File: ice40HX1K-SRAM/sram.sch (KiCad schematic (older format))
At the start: 1 part

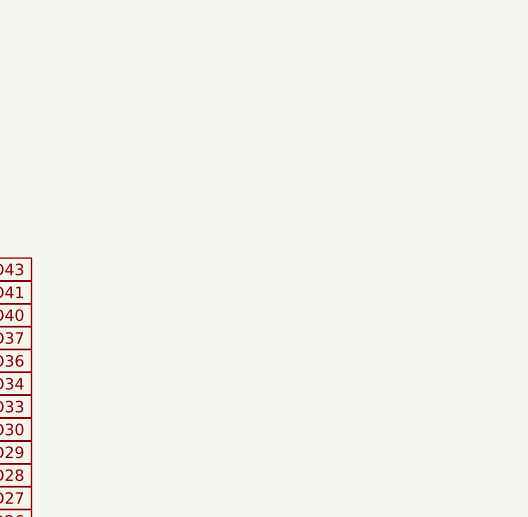
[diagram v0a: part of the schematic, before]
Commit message: Started USB => ice40 HX1K Bridge with ATSAMD11C14A
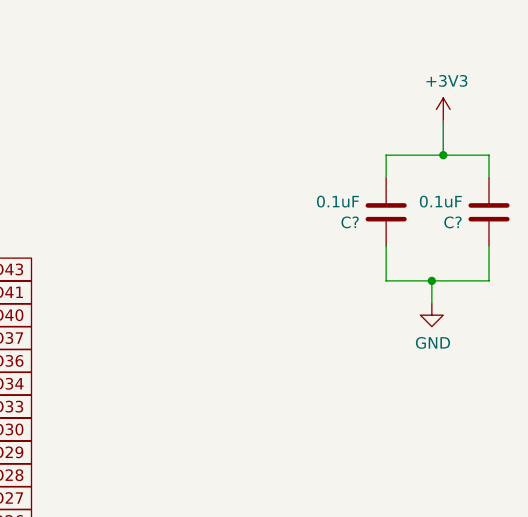
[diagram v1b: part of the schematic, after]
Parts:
- added C? (x2): 0.1uF, Capacitor_SMD:C_0805_2012Metric, symbol Device:C
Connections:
- net +3V3: now also C?.2, C?.2
- net GND: now also C?.1, C?.1
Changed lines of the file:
@@
 $Descr A4 11693 8268
 encoding utf-8
-Sheet 6 6
+Sheet 6 8
 Title ""
 Date ""
@@
 	1750 1550 1750 2600
 NoConn ~ 3450 4050
+$Comp
+L Device:C C?
+U 1 1 5E6179A9
+P 6050 2400
+AR Path="/5E6179A9" Ref="C?"  Part="1"
+AR Path="/5E5F7D61/5E6179A9" Ref="C?"  Part="1"
+F 0 "C?" H 6165 2446 50  0000 L CNN
+F 1 "0.1uF" H 6165 2355 50  0000 L CNN
+F 2 "Capacitor_SMD:C_0805_2012Metric" H 6088 2250 50  0001 C CNN
+F 3 "~" H 6050 2400 50  0001 C CNN
+	1    6050 2400
+	-1   0    0    1
+$EndComp
+$Comp
+L Device:C C?
+U 1 1 5E6179AF
+P 6500 2400
+AR Path="/5E6179AF" Ref="C?"  Part="1"
+AR Path="/5E5F7D61/5E6179AF" Ref="C?"  Part="1"
+F 0 "C?" H 6615 2446 50  0000 L CNN
+F 1 "0.1uF" H 6615 2355 50  0000 L CNN
+F 2 "Capacitor_SMD:C_0805_2012Metric" H 6538 2250 50  0001 C CNN
+F 3 "~" H 6500 2400 50  0001 C CNN
+	1    6500 2400
+	-1   0    0    1
+$EndComp
+$Comp
+L power:GND #PWR?
+U 1 1 5E6179B5
+P 6250 2800
+AR Path="/5E6179B5" Ref="#PWR?"  Part="1"
+AR Path="/5E5F7D61/5E6179B5" Ref="#PWR?"  Part="1"
+F 0 "#PWR?" H 6250 2550 50  0001 C CNN
+F 1 "GND" H 6255 2627 50  0000 C CNN
+F 2 "" H 6250 2800 50  0001 C CNN
+F 3 "" H 6250 2800 50  0001 C CNN
+	1    6250 2800
+	1    0    0    -1
+$EndComp
+$Comp
+L power:+3V3 #PWR?
+U 1 1 5E6179BB
+P 6300 2000
+AR Path="/5E6179BB" Ref="#PWR?"  Part="1"
+AR Path="/5E5F7D61/5E6179BB" Ref="#PWR?"  Part="1"
+F 0 "#PWR?" H 6300 1850 50  0001 C CNN
+F 1 "+3V3" H 6315 2173 50  0000 C CNN
+F 2 "" H 6300 2000 50  0001 C CNN
+F 3 "" H 6300 2000 50  0001 C CNN
+	1    6300 2000
+	1    0    0    -1
+$EndComp
+Wire Wire Line
+	6050 2550 6050 2700
+Wire Wire Line
+	6050 2700 6250 2700
+Wire Wire Line
+	6250 2700 6250 2800
+Wire Wire Line
+	6250 2700 6500 2700
+Connection ~ 6250 2700
+Wire Wire Line
+	6500 2250 6500 2150
+Wire Wire Line
+	6500 2150 6300 2150
+Wire Wire Line
+	6300 2150 6300 2000
+Wire Wire Line
+	6050 2250 6050 2150
+Wire Wire Line
+	6050 2150 6300 2150
+Connection ~ 6300 2150
+Wire Wire Line
+	6500 2550 6500 2700
 $EndSCHEMATC
